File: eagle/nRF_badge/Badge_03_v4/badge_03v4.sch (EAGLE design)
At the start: 45 parts, among them J1 PROG_CONN_6, U1 AT25M02, U2 LP2985LV, U3 MCP6231, U4 PCF85263, Y1 32768Hz, Y2 32768Hz

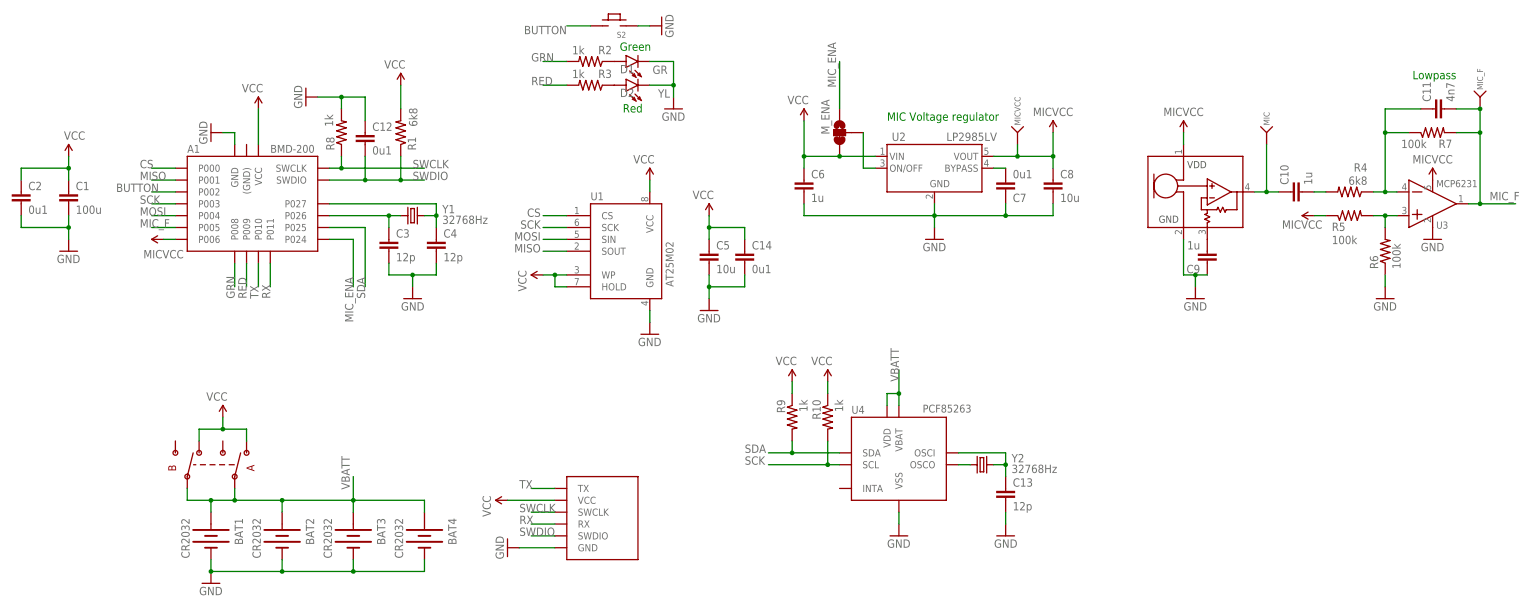
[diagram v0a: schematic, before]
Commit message: Added ULPs to generate BOM and centroid data; post-processed BOM with Digikey part #'s
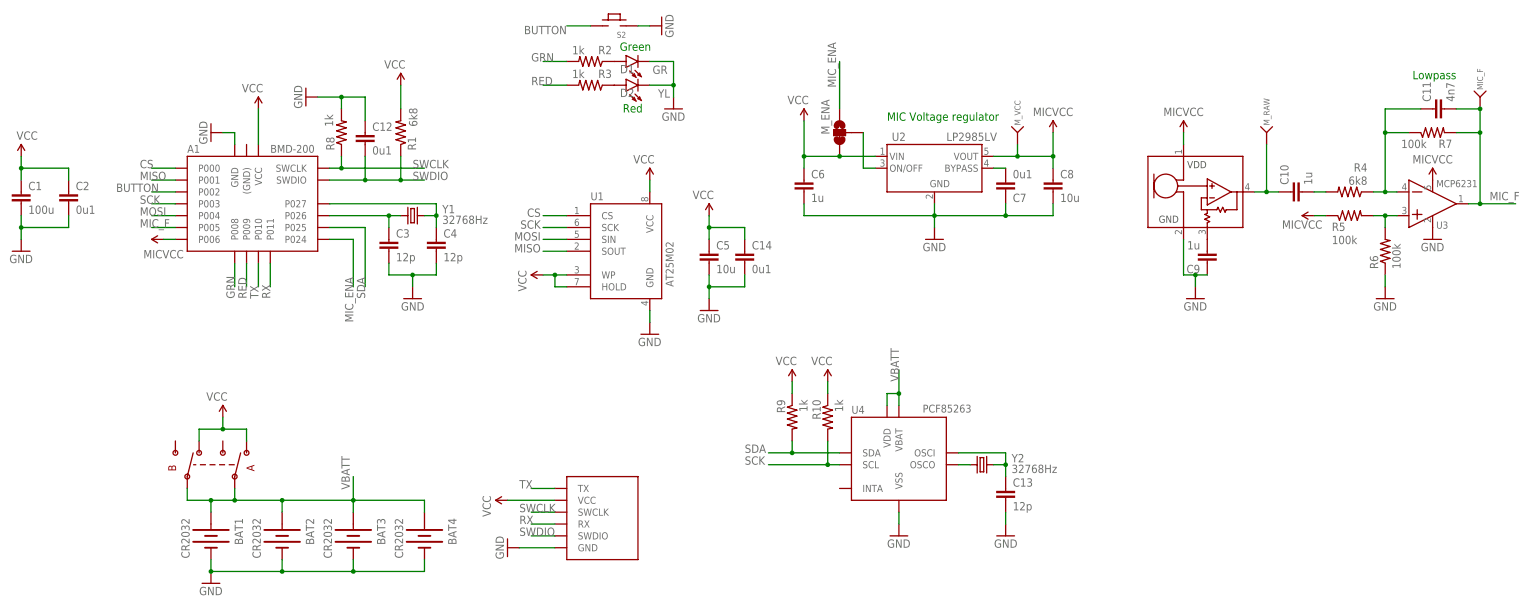
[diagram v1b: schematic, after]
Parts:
- MK1: value SPU0414(AMP) -> SPU0414
- S1: value JS202011SCQN -> DPDT
- S2: value TACT6MM4 -> TACT6mm
- renumbered MIC to M_RAW, MICVCC to M_VCC
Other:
- moved on the sheet: C1, C2
